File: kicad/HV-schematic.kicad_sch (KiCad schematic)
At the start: 13 parts, among them J1 Power JST, J3 Brake motor JST, U0 Relay, U1 ESCON_module-50/5, U2 A4988

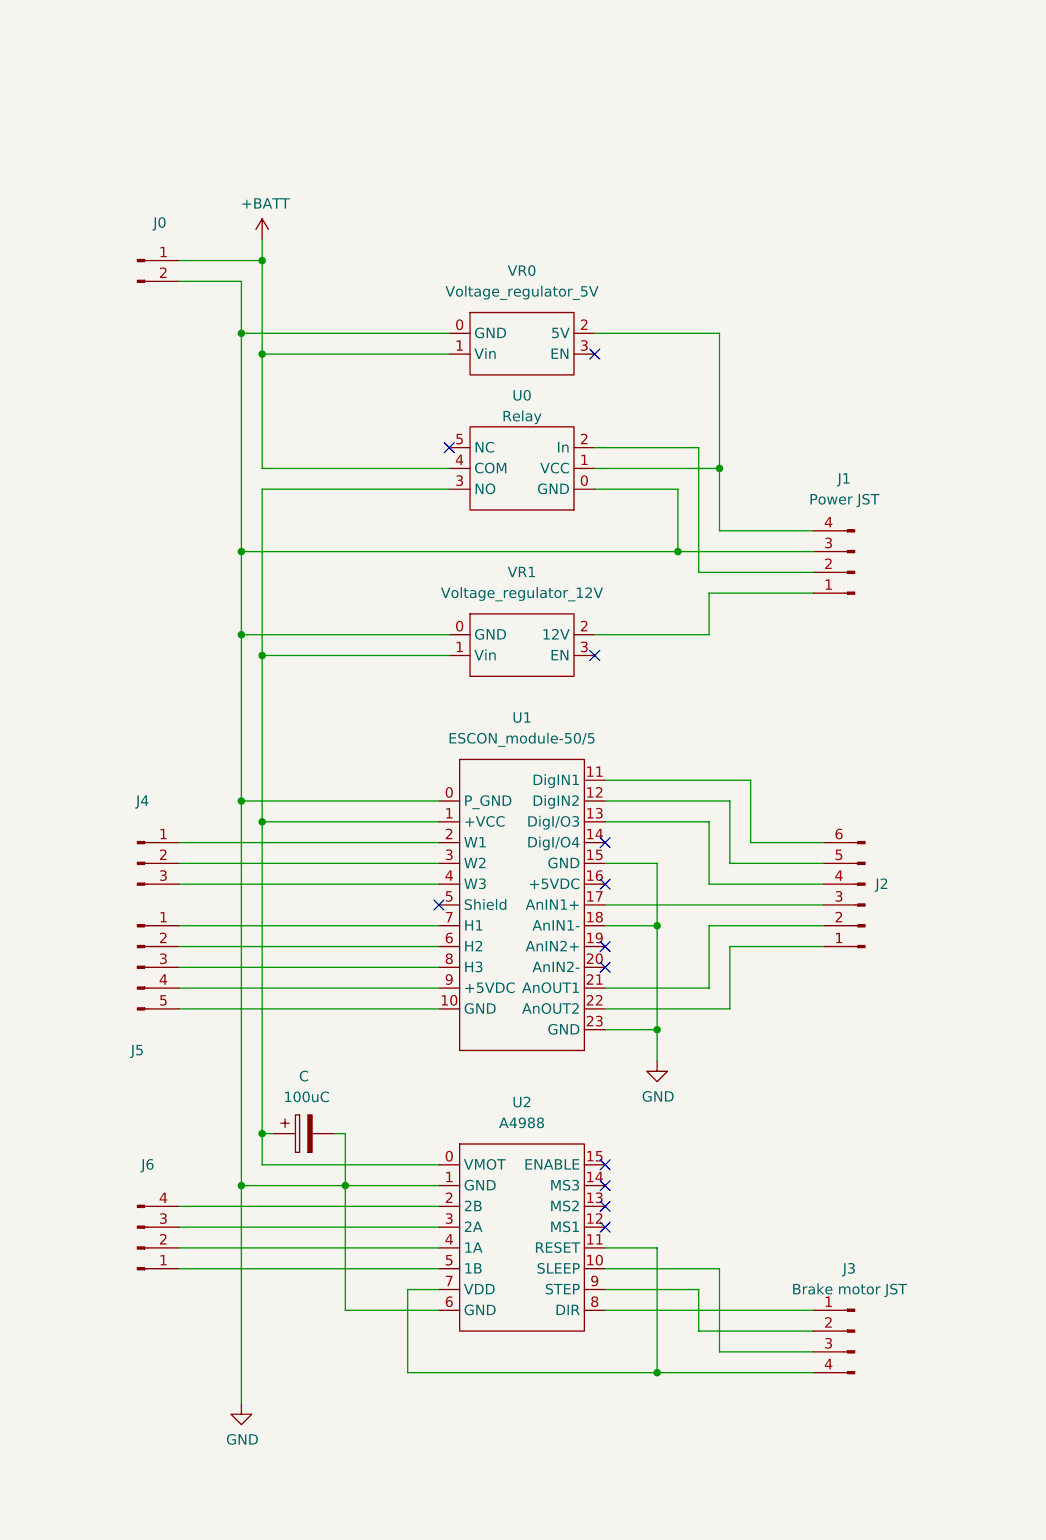
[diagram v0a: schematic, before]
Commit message: Update kicad
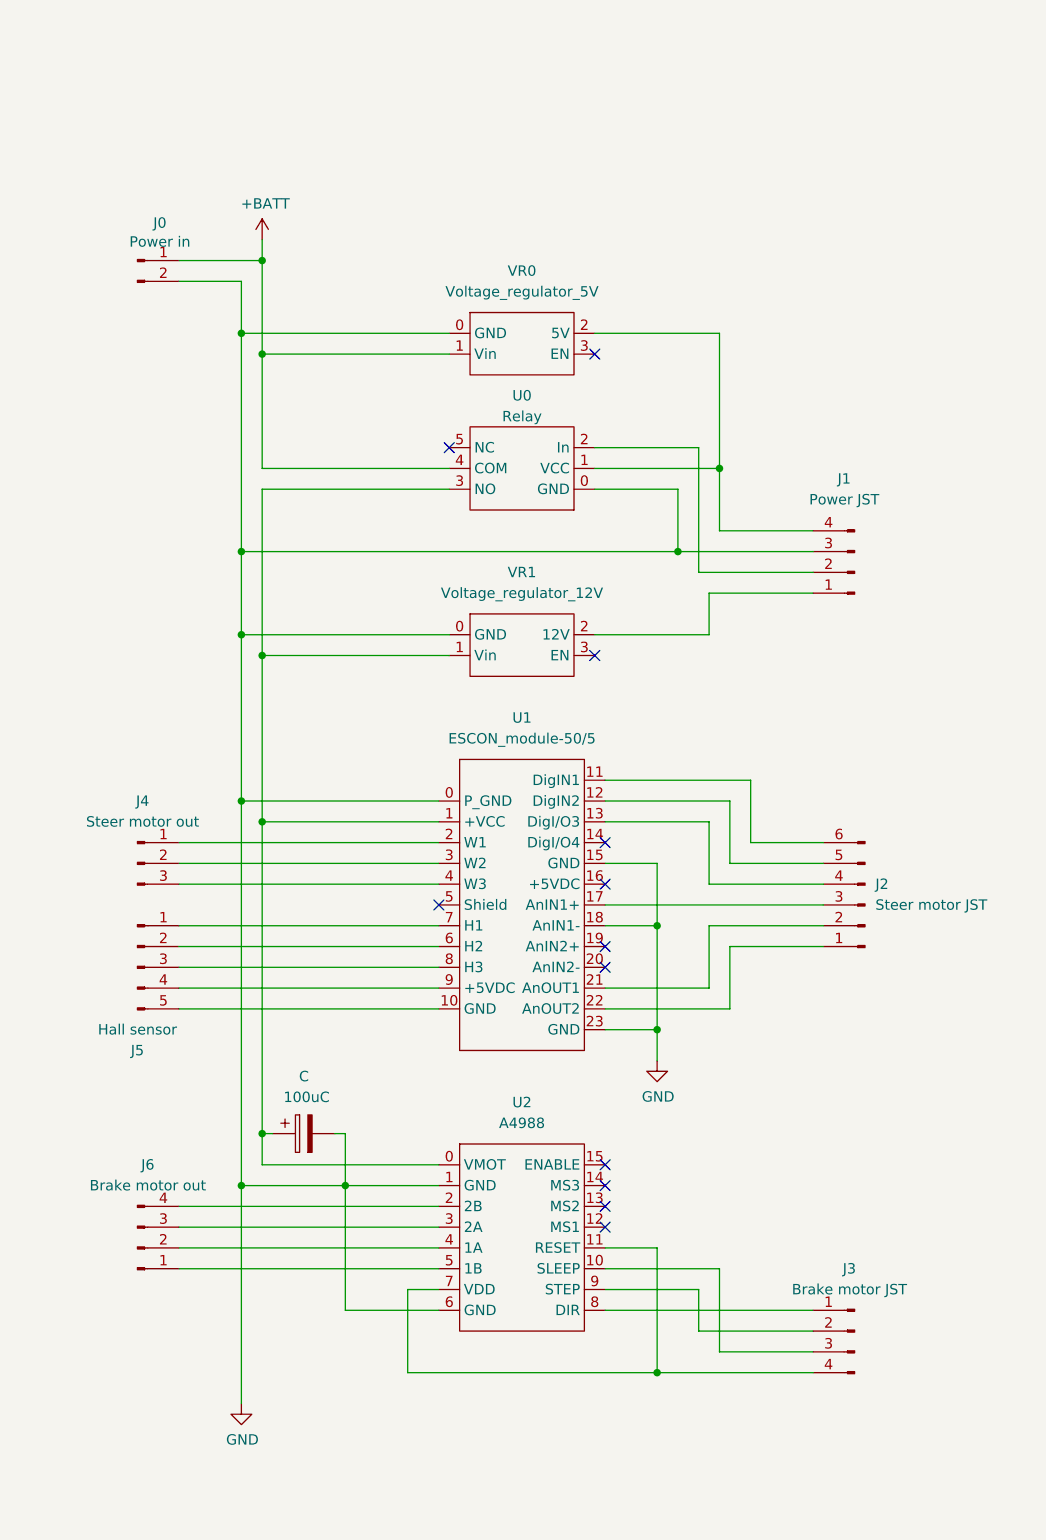
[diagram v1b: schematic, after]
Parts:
- J0: value (none) -> Power in
- J2: value (none) -> Steer motor JST
- J4: value (none) -> Steer motor out
- J5: value (none) -> Hall sensor
- J6: value (none) -> Brake motor out
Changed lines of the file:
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@@
     (in_bom yes) (on_board yes)
     (property "Reference" "J6" (id 0) (at 60.96 171.45 0))
-    (property "Value" "" (id 1) (at 60.96 173.99 0))
+    (property "Value" "Brake motor out" (id 1) (at 60.96 173.99 0))
     (property "Footprint" "" (id 2) (at 59.69 181.61 0)
       (effects (font (size 1.27 1.27)) hide)
@@
     (in_bom yes) (on_board yes)
     (property "Reference" "J0" (id 0) (at 62.4332 56.3626 0))
-    (property "Value" "" (id 1) (at 62.4332 58.674 0))
+    (property "Value" "Power in" (id 1) (at 62.4332 58.674 0))
     (property "Footprint" "TerminalBlock:TerminalBlock_bornier-2_P5.08mm" (id 2) (at 59.69 60.96 0)
       (effects (font (size 1.27 1.27)) hide)
@@
       (effects (font (size 1.27 1.27)) (justify right))
     )
-    (property "Value" "" (id 1) (at 149.86 139.6999 0)
+    (property "Value" "Steer motor JST" (id 1) (at 149.86 139.6999 0)
       (effects (font (size 1.27 1.27)) (justify right))
     )
@@
     (in_bom yes) (on_board yes)
     (property "Reference" "J5" (id 0) (at 59.69 157.48 0))
-    (property "Value" "" (id 1) (at 59.69 154.94 0))
+    (property "Value" "Hall sensor" (id 1) (at 59.69 154.94 0))
     (property "Footprint" "" (id 2) (at 59.69 147.32 0)
       (effects (font (size 1.27 1.27)) hide)
@@
     (in_bom yes) (on_board yes) (fields_autoplaced)
     (property "Reference" "J4" (id 0) (at 60.325 127 0))
-    (property "Value" "" (id 1) (at 60.325 129.54 0))
+    (property "Value" "Steer motor out" (id 1) (at 60.325 129.54 0))
     (property "Footprint" "" (id 2) (at 59.69 134.62 0)
       (effects (font (size 1.27 1.27)) hide)

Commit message: Update kicad and doc
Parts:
- added J16: Power mtr out, TerminalBlock:TerminalBlock_bornier-2_P5.08mm, symbol Connector:Conn_01x02_Male
- added J17: Power mtr in, symbol Connector:Conn_01x02_Male
- J10: renamed from J1; footprint (none) -> Connector_JST_inches:JST_1x04_P2.54
- J11: renamed from J2; value Steer motor JST -> Steer mtr JST
- J12: renamed from J3; value Brake motor JST -> Brake mtr JST; footprint (none) -> Connector_JST_inches:JST_1x04_P2.54
- J13: renamed from J4; value Steer motor out -> Steer mtr out
- J15: renamed from J6; value Brake motor out -> Brake mtr out; footprint (none) -> Connector_JST_inches:JST_1x04_P2.54
- J9: renamed from J0; value Power in -> Bat in
- U11: renamed from U2; value A4988 -> (none)
- U9: renamed from U0; value Relay -> (none)
- renumbered C to C1, J5 to J14, U1 to U10
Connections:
- net +BATT: now also U9.5 (COM), VR0.2 (Vin); no longer U9.4 (COM), VR0.1 (Vin)
- net GND: now also U10.1 (Shield), U10.16 (AnIN1-), U11.9 (GND), U9.1 (GND), VR0.1 (GND), VR1.1 (GND), J16.2 (Pin_2); no longer U10.0 (P_GND), U10.15 (GND), U10.18 (AnIN1-), U10.23 (GND), U11.1 (GND), U11.6 (GND), U9.0 (GND), VR0.0 (GND), VR1.0 (GND)
- net at U9.2 (VCC): now also J10.4 (Pin_4), VR0.3 (5V); no longer J10.2 (Pin_2)
- net at J15.1 (Pin_1): now also U11.11 (1B); no longer U11.5 (1B)
- net at J15.2 (Pin_2): now also U11.12 (1A); no longer U11.4 (1A)
- net at J15.3 (Pin_3): now also U11.13 (2A); no longer U11.3 (2A)
- net at J15.4 (Pin_4): now also U11.14 (2B); no longer U11.2 (2B)
- net at J14.5 (Pin_5): now also U10.1 (Shield); no longer U10.10 (GND)
- net at J11.6 (Pin_6): now also U10.10 (DigIN1); no longer U10.11 (DigIN1)
- net at J11.5 (Pin_5): now also U10.11 (DigIN2); no longer U10.12 (DigIN2)
- net at J11.4 (Pin_4): now also U10.12 (DigI/O3); no longer U10.13 (DigI/O3)
- net at J11.3 (Pin_3): now also U10.15 (AnIN1+); no longer U10.17 (AnIN1+)
- net at U10.19 (AnOUT1): now also J11.2 (Pin_2)
- net at U10.2 (+VCC): now also J17.2 (Pin_2); no longer J13.1 (Pin_1)
- net at U10.20 (AnOUT2): now also J11.1 (Pin_1)
- net at U10.3 (W1): now also J13.1 (Pin_1); no longer J13.2 (Pin_2)
- net at U10.4 (W2): now also J13.2 (Pin_2); no longer J13.3 (Pin_3)
- net at U10.5 (W3): now also J13.3 (Pin_3)
- net at U10.6 (H1): now also J14.1 (Pin_1); no longer J14.2 (Pin_2)
- net at U10.7 (H2): now also J14.2 (Pin_2); no longer J14.1 (Pin_1)
- net at U11.10 (VDD): now also J12.4 (Pin_4), U11.5 (RESET); no longer J12.3 (Pin_3)
- net at U11.15 (VMOT): now also C1.1, U9.6 (NO), VR1.2 (Vin), J16.1 (Pin_1)
- net at J12.2 (Pin_2): now also U11.7 (STEP); no longer U11.9 (STEP)
- net at J10.1 (Pin_1): now also VR1.3 (12V); no longer VR1.2 (12V)
- new net: J10.2 (Pin_2), U9.3 (In)
- new net: J17.1 (Pin_1), U10.1 (Shield)
- new net: J12.3 (Pin_3), U11.6 (SLEEP)
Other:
- moved on the sheet: C1, J10, J11, J12, J13, J14, J15, J9, U10, U11, U9, VR0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

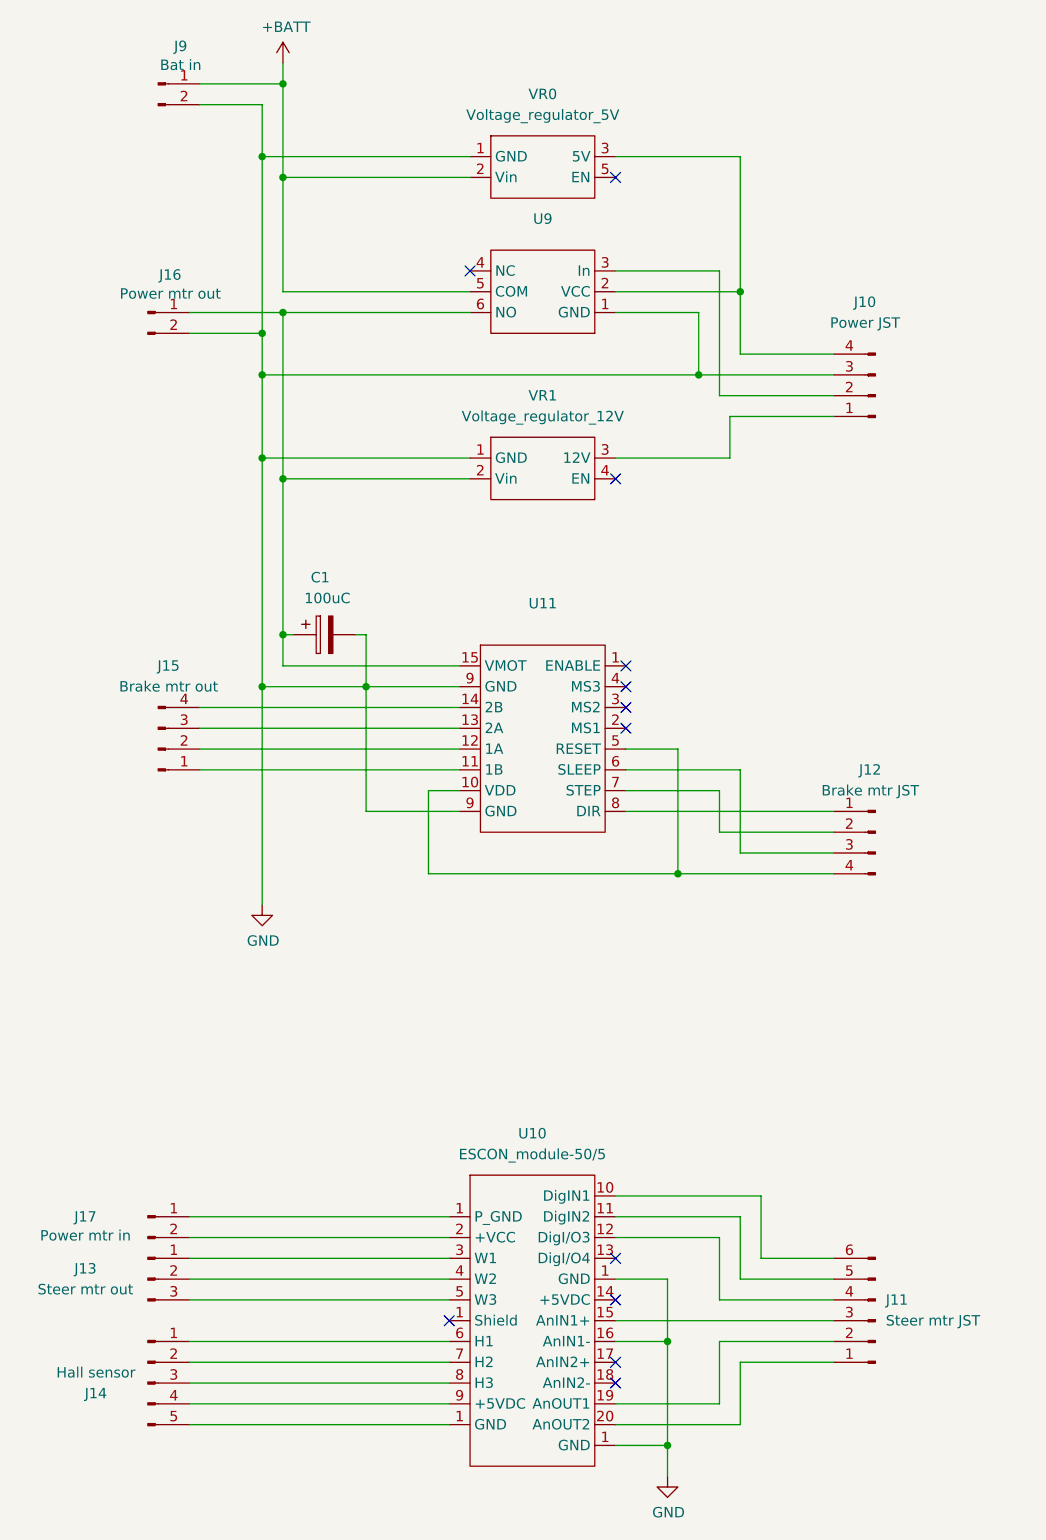
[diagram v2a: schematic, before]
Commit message: Update kicad
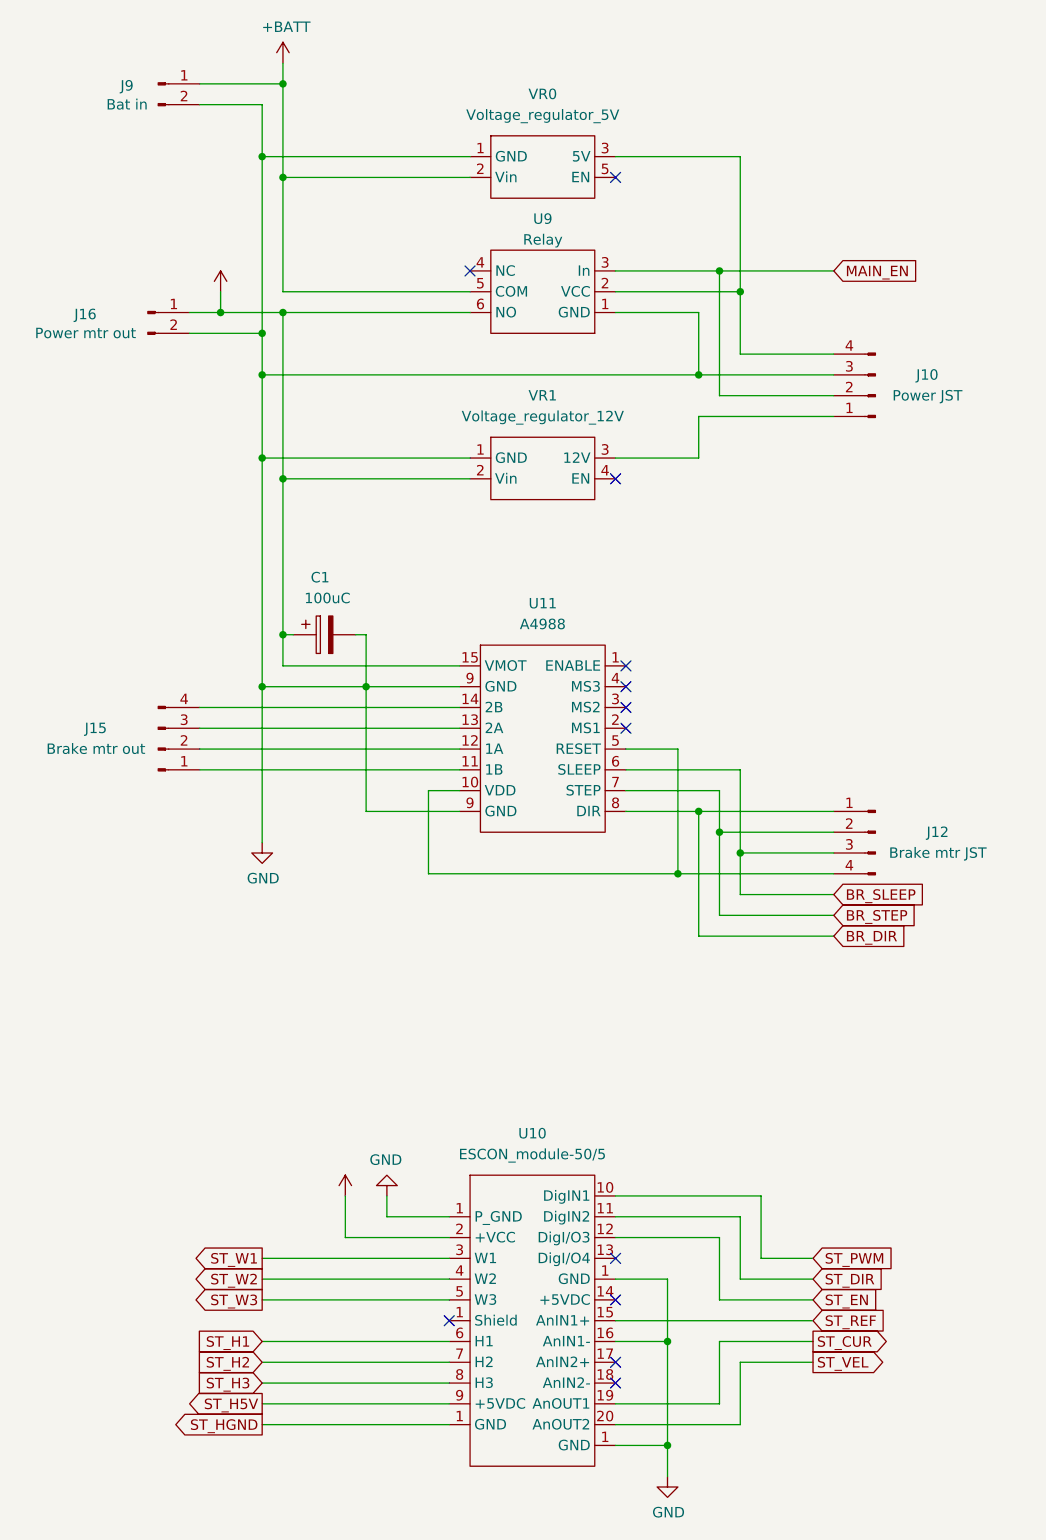
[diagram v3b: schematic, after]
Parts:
- removed J11: Steer mtr JST, symbol Connector:Conn_01x06_Male
- removed J13: Steer mtr out, symbol Connector:Conn_01x03_Male
- removed J14: Hall sensor, symbol Connector:Conn_01x05_Male
- removed J17: Power mtr in, symbol Connector:Conn_01x02_Male
- U10: footprint (none) -> SBBMicro:Escon module-50-5
- U11: value (none) -> A4988; footprint (none) -> SBBMicro:A4988
- U9: value (none) -> Relay; footprint (none) -> SBBMicro:Relay
- VR0: footprint (none) -> SBBMicro:Voltage-reg_5V
- VR1: footprint (none) -> SBBMicro:Voltage-reg_12V
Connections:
- net MAIN_EN: now reaches J10.2 (Pin_2), U9.3 (In)
- net +24V: now reaches C1.1, J16.1 (Pin_1), U11.15 (VMOT), U9.6 (NO), VR1.2 (Vin)
- net +24V: now also U10.2 (+VCC)
- net ST_HGND: now reaches U10.1 (Shield)
- net ST_PWM: now reaches U10.10 (DigIN1)
- net ST_DIR: now reaches U10.11 (DigIN2)
- net ST_EN: now reaches U10.12 (DigI/O3)
- net ST_REF: now reaches U10.15 (AnIN1+)
- net ST_CUR: now reaches U10.19 (AnOUT1)
- net ST_VEL: now reaches U10.20 (AnOUT2)
- net ST_W1: now reaches U10.3 (W1)
- net ST_W2: now reaches U10.4 (W2)
- net ST_W3: now reaches U10.5 (W3)
- net ST_H1: now reaches U10.6 (H1)
- net ST_H2: now reaches U10.7 (H2)
- net ST_H3: now reaches U10.8 (H3)
- net ST_H5V: now reaches U10.9 (+5VDC)
- net BR_SLEEP: now reaches J12.3 (Pin_3), U11.6 (SLEEP)
- net BR_STEP: now reaches J12.2 (Pin_2), U11.7 (STEP)
- net BR_DIR: now reaches J12.1 (Pin_1), U11.8 (DIR)
